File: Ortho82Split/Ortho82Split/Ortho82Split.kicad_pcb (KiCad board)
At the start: 2 copper layers, 147.9 x 134.5 mm, 117 parts, among them J1 Left-Right, J3 USB_C_Receptacle_USB2.0, J9 TC2030-IDC-NL, SW11 SW_Push, SW12 SW_Push, SW13 SW_Push, SW14 SW_Push, SW15 SW_Push, SW16 SW_Push, SW17 SW_Push, SW18 SW_Push, SW19 SW_Push, SW20 SW_Push, SW21 SW_Push, SW22 SW_Push, SW23 SW_Push, SW24 SW_Push, SW25 SW_Push, SW26 SW_Push, SW27 SW_Push, SW28 SW_Push, SW29 SW_Push, SW30 SW_Push, SW31 SW_Push, SW32 SW_Push, SW33 SW_Push, SW34 SW_Push, SW35 SW_Push, SW36 SW_Push, SW37 SW_Push, SW38 SW_Push, SW39 SW_Push, SW40 SW_Push, SW41 SW_Push, SW42 SW_Push, SW43 SW_Push, SW44 SW_Push, SW45 SW_Push, SW46 SW_Push, SW47 SW_Push, SW48 SW_Push, SW49 SW_Push, SW50 SW_Push, SW51 SW_Push, SW74 Left/Right, SW83 ~{RESET}, U1 MCP1700T-3302E_TT, U2 ATxmega32A4U-A, U3 USBLC6-2SC6

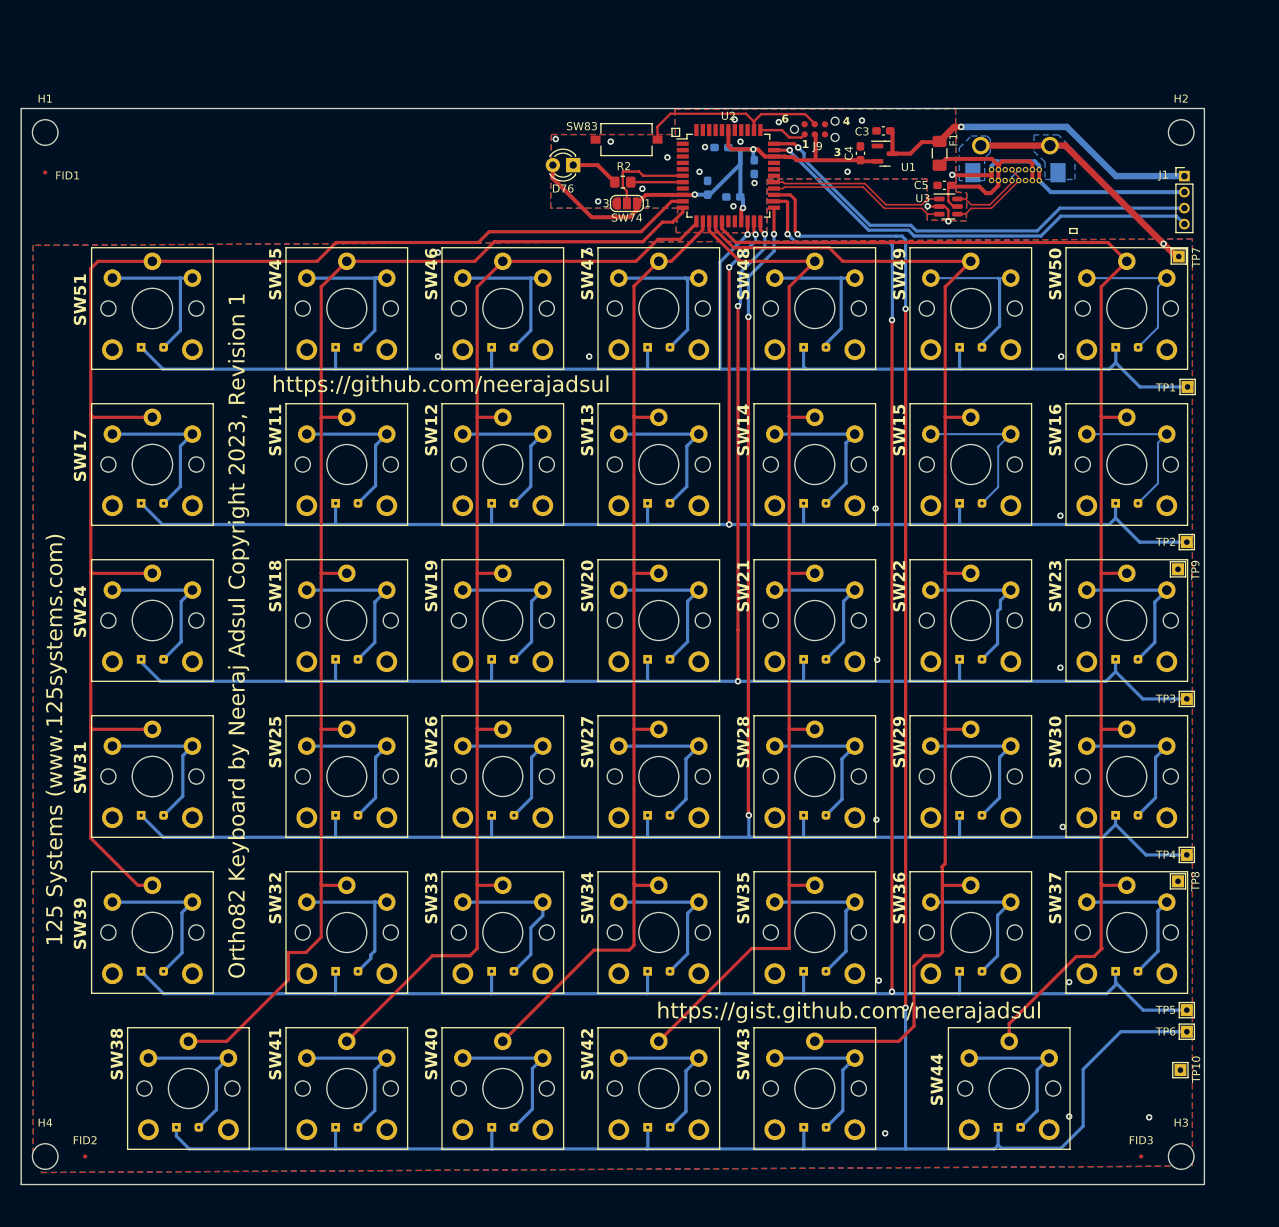
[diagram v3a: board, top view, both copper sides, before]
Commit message: Adds USB current resistors.
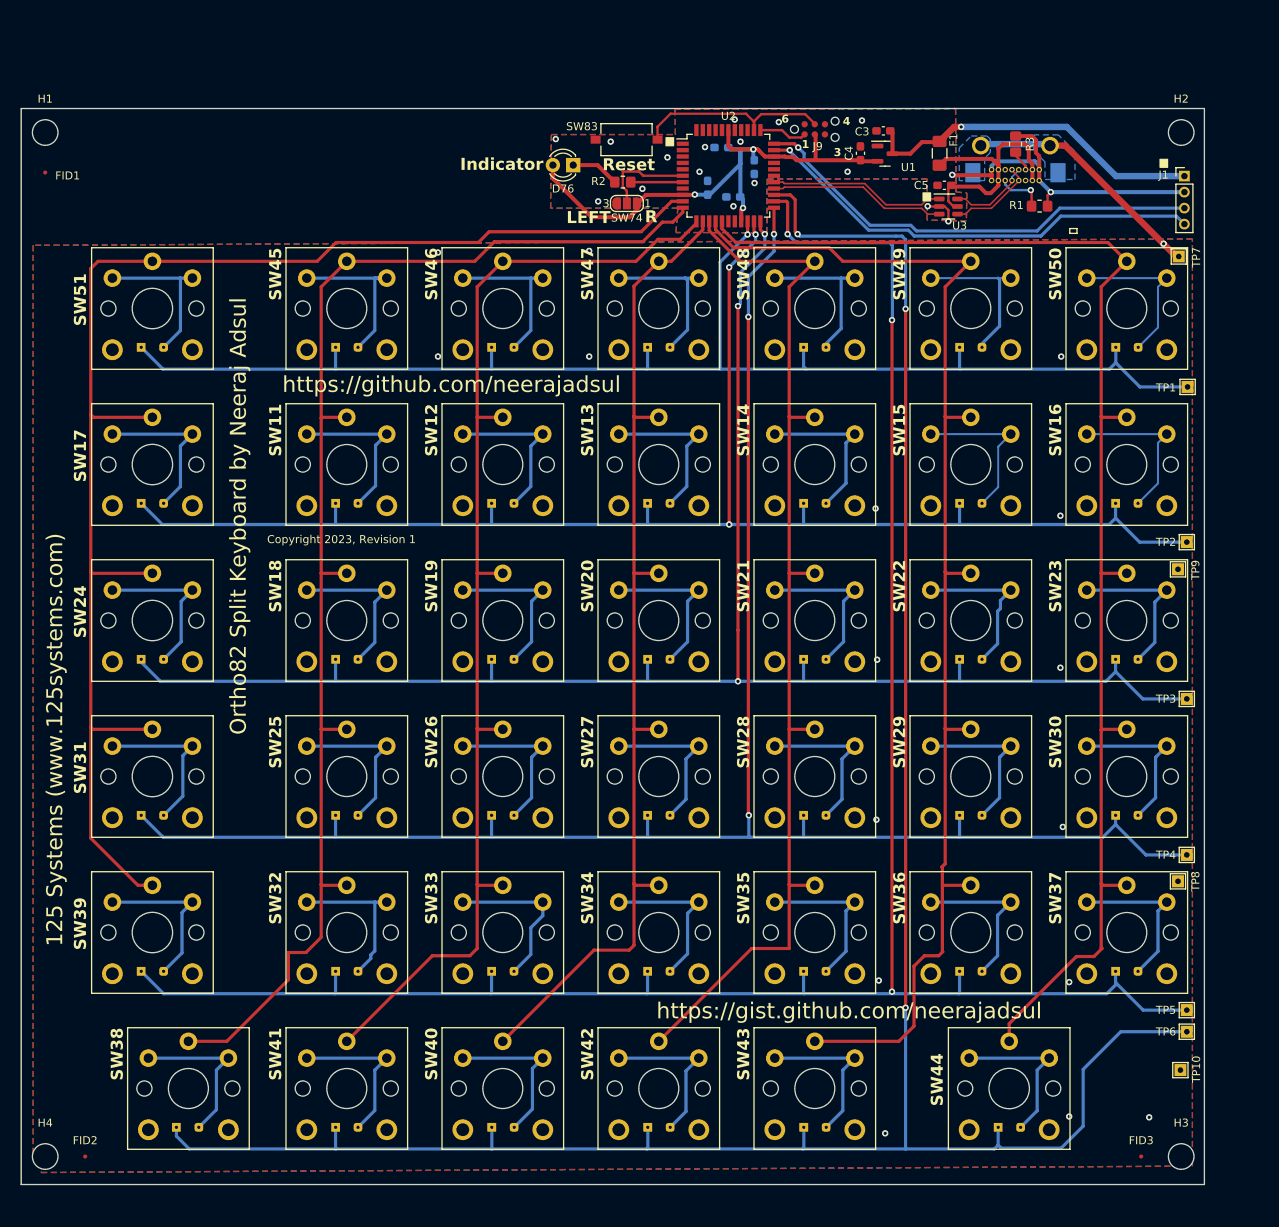
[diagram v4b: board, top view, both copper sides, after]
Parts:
- added R1: 5.1k, Resistor_SMD:R_0805_2012Metric_Pad1.20x1.40mm_HandSolder, F.Cu at (166.3, 52.2)
- added R3: 5.1k, Resistor_SMD:R_0805_2012Metric_Pad1.20x1.40mm_HandSolder, F.Cu at (163.3, 44.5)
- C1, C2, C6, C7: value C -> 100n
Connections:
- J3 pad A5: unconnected-(J3-CC1-PadA5) -> Net-(J3-CC1)
- J3 pad B5: unconnected-(J3-CC2-PadB5) -> Net-(J3-CC2)
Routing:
- net GND: track 38.0 -> 46.5 mm, vias 17 -> 18
- net Net-(J3-CC1): track 0.00 -> 5.43 mm, vias 0 -> 1
- net /VBUS: track 28.0 -> 32.0 mm
- net Net-(J3-CC2): track 0.00 -> 2.72 mm
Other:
- board text added: "Copyright 2023, Revision 1"
- board text added: "Indicator"
- board text added: "LEFT"
- board text added: "Ortho82 Split Keyboard by Neeraj Adsul"
- board text added: "R"
- board text added: "Reset"
- board text removed: "Ortho82 Keyboard by Neeraj Adsul Copyright 2023, Revision 1"

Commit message: Adds reference footprints in empty space.
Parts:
- added 0402: C_0402_1005Metric, Capacitor_SMD:C_0402_1005Metric, F.Cu at (47.9, 41.5)
- added 0603: C_0603_1608Metric, Capacitor_SMD:C_0603_1608Metric, F.Cu at (47.9, 42.9)
- added 0805: C_0805_2012Metric, Capacitor_SMD:C_0805_2012Metric, F.Cu at (47.8, 44.8)
- added 1.27: PinHeader_1x06_P1.27mm_Vertical, Connector_PinHeader_1.27mm:PinHeader_1x06_P1.27mm_Vertical, F.Cu at (78.8, 44.7)
- added 1206: C_1206_3216Metric, Capacitor_SMD:C_1206_3216Metric, F.Cu at (48.0, 47.1)
- added 1210: C_1210_3225Metric, Capacitor_SMD:C_1210_3225Metric, F.Cu at (48.0, 50.1)
- added 1812: C_1812_4532Metric, Capacitor_SMD:C_1812_4532Metric, F.Cu at (48.2, 53.9)
- added 1mm: PinHeader_1x08_P1.00mm_Vertical, Connector_PinHeader_1.00mm:PinHeader_1x08_P1.00mm_Vertical, F.Cu at (78.6, 41.9)
- added 2.54: PinHeader_1x04_P2.54mm_Vertical, Connector_PinHeader_2.54mm:PinHeader_1x04_P2.54mm_Vertical, F.Cu at (78.6, 52.1)
- added 2mm: PinHeader_1x05_P2.00mm_Vertical, Connector_PinHeader_2.00mm:PinHeader_1x05_P2.00mm_Vertical, F.Cu at (78.3, 48.3)
- added 3214G: Potentiometer_Bourns_3214G_Horizontal, Potentiometer_SMD:Potentiometer_Bourns_3214G_Horizontal, B.Cu at (93.4, 53.4)
- added 3224W: Potentiometer_Bourns_3224W_Vertical, Potentiometer_SMD:Potentiometer_Bourns_3224W_Vertical, B.Cu at (102.2, 44.7)
- added 3314R: Potentiometer_Bourns_3314R-GM5_Vertical, Potentiometer_SMD:Potentiometer_Bourns_3314R-GM5_Vertical, B.Cu at (100.3, 52.1)
- added 6.3x5.4: CP_Elec_6.3x5.4_Nichicon, Capacitor_SMD:CP_Elec_6.3x5.4_Nichicon, B.Cu at (94.1, 45.6)
- added LQFP48: LQFP-48-1EP_7x7mm_P0.5mm_EP3.6x3.6mm, Package_QFP:LQFP-48-1EP_7x7mm_P0.5mm_EP3.6x3.6mm, B.Cu at (70.1, 47.2)
- added MSOP-8: MSOP-8-1EP_3x3mm_P0.65mm_EP1.68x1.88mm, Package_SO:MSOP-8-1EP_3x3mm_P0.65mm_EP1.68x1.88mm, F.Cu at (64.7, 43.3)
- added MSOP16: MSOP-16-1EP_3x4.039mm_P0.5mm_EP1.651x2.845mm, Package_SO:MSOP-16-1EP_3x4.039mm_P0.5mm_EP1.651x2.845mm, F.Cu at (64.8, 50.6)
- added PLCC6: LED_RGB_PLCC-6, LED_SMD:LED_RGB_PLCC-6, F.Cu at (42.5, 53.9)
- added QFN32: QFN-32-1EP_5x5mm_P0.5mm_EP3.1x3.1mm, Package_DFN_QFN:QFN-32-1EP_5x5mm_P0.5mm_EP3.1x3.1mm, B.Cu at (48.6, 45.3)
- added QFN48: QFN-48-1EP_7x7mm_P0.5mm_EP5.3x5.3mm, Package_DFN_QFN:QFN-48-1EP_7x7mm_P0.5mm_EP5.3x5.3mm, B.Cu at (48.9, 52.7)
- added QFN64: QFN-64-1EP_9x9mm_P0.5mm_EP3.4x3.4mm, Package_DFN_QFN:QFN-64-1EP_9x9mm_P0.5mm_EP3.4x3.4mm, B.Cu at (58.3, 47.4)
- added SC-59: SC-59, Package_TO_SOT_SMD:SC-59, F.Cu at (56.8, 42.8)
- added SC-70: SC-70-8, Package_TO_SOT_SMD:SC-70-8, F.Cu at (56.6, 46.3)
- added SO-8: SO-8_3.9x4.9mm_P1.27mm, Package_SO:SO-8_3.9x4.9mm_P1.27mm, F.Cu at (72.3, 44.2)
- added SOT-89-5: SOT-89-5, Package_TO_SOT_SMD:SOT-89-5, F.Cu at (56.5, 50.3)
- added Scale: Gauge_10mm_Type2_CopperTop, Calibration_Scale:Gauge_10mm_Type2_CopperTop, F.Cu at (93.5, 51.4)
- added VSON-10: VSON-10-1EP_3x3mm_P0.5mm_EP1.2x2mm, Package_SON:VSON-10-1EP_3x3mm_P0.5mm_EP1.2x2mm, F.Cu at (72.0, 51.0)
- added WSON-10: WSON-10-1EP_2.5x2.5mm_P0.5mm_EP1.2x2mm, Package_SON:WSON-10-1EP_2.5x2.5mm_P0.5mm_EP1.2x2mm, F.Cu at (98.2, 46.3)
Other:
- board text added: "0.5mm"
- board text added: "0.65mm"
- board text added: "1.27"
- board text added: "LED"
- board text removed: "Indicator"
